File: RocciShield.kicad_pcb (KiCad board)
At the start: 2 copper layers, 176 parts, among them J1 Battery, J10 M3, J11 I2C6, J12 M4, J13 I2C7, J14 Power, J2 I2C0, J3 I2C1, J4 I2C2, J5 I2C3, J6 M1, J7 I2C4, J8 M2, J9 I2C5, Q1 IRF7416, U1 LMR33630, U2 AMS1117-3.3, U3 L7808, U4 TPS3700, U5 TCA9548A, U6 DRV8871, U7 DRV8871, U8 DRV8871, U9 DRV8871

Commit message: change linear regulator to lm317 (jlc basic part)
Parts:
- removed F10, F12, F13, F15, F16, F18, F19, F21, F22, F24, F25, F3, F4, F6, F7, F9: 10 mA, Fuse:Fuse_0805_2012Metric
- removed U3: L7808, Package_TO_SOT_SMD:SOT-223-3_TabPin2
- added R62: 1k, Resistor_SMD:R_0603_1608Metric, F.Cu at (205.5, 64.5)
- added U10: LM317_TO-252, Package_TO_SOT_SMD:TO-252-2, F.Cu at (210.4, 59.2)
- C1: value 10µ -> 22µ
- C13: value 100µ -> 22µ
- F1, F11, F14, F17, F20, F23, F5, F8: value 100 mA -> 1 A
- R12: value 200 -> 330
- R13: value 20 -> 150
- R28: value 20 -> 270
- U2: value AMS1117-3.3 -> LM317_TO-252; footprint Package_TO_SOT_SMD:SOT-223-3_TabPin2 -> Package_TO_SOT_SMD:TO-252-2
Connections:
- D17 pad 2: ERROR_LED -> +5V
- R28 pad 2: GND -> Net-(Q2-S)
- U2 pad 1: GND -> Net-(U2-ADJ)

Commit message: added changes from #2
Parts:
- removed F14, F17, F20, F23: 1 A, Fuse:Fuse_0805_2012Metric
- removed F26: 3A, Fuse:Fuse_1812_4532Metric
- removed F27: 1A, Fuse:Fuse_1812_4532Metric
- removed U10: LM317_TO-252, Package_TO_SOT_SMD:TO-252-2
- added C19: 100n, Capacitor_SMD:C_0603_1608Metric, F.Cu at (139.8, 54.3)
- added F10: 300 mA ptc, Fuse:Fuse_0805_2012Metric, F.Cu at (90.4, 143.7)
- added F3: 300 mA ptc, Fuse:Fuse_0805_2012Metric, F.Cu at (91.0, 56.1)
- added F4: 300 mA ptc, Fuse:Fuse_0805_2012Metric, F.Cu at (91.0, 70.7)
- added F6: 300 mA ptc, Fuse:Fuse_0805_2012Metric, F.Cu at (90.4, 100.5)
- added F7: 300 mA ptc, Fuse:Fuse_0805_2012Metric, F.Cu at (90.4, 115.1)
- added F9: 3A ptc, Fuse:Fuse_2920_7451Metric, F.Cu at (35.8, 143.7)
- added Q2: 2N7002, Package_TO_SOT_SMD:SOT-23, F.Cu at (28.1, 117.7)
- added R42: 1k, Resistor_SMD:R_0603_1608Metric, F.Cu at (248.7, 104.8)
- added R43: 30k, Resistor_SMD:R_0805_2012Metric, F.Cu at (240.4, 109.2)
- added R44: 4k7, Resistor_SMD:R_0603_1608Metric, F.Cu at (65.6, 120.2)
- added R45: 4k7, Resistor_SMD:R_0603_1608Metric, F.Cu at (69.4, 120.2)
- added R46: 1k, Resistor_SMD:R_0603_1608Metric, F.Cu at (31.9, 120.9)
- added R47: 100, Resistor_SMD:R_0603_1608Metric, F.Cu at (85.3, 123.4)
- added R48: 100, Resistor_SMD:R_0603_1608Metric, F.Cu at (85.3, 126.6)
- added R49: 1k, Resistor_SMD:R_0603_1608Metric, F.Cu at (244.8, 120.0)
- added R50: 1k, Resistor_SMD:R_0603_1608Metric, F.Cu at (248.7, 120.0)
- added R51: 30k, Resistor_SMD:R_0805_2012Metric, F.Cu at (240.4, 124.5)
- added R52: 4k7, Resistor_SMD:R_0603_1608Metric, F.Cu at (65.6, 134.2)
- added R53: 4k7, Resistor_SMD:R_0603_1608Metric, F.Cu at (69.4, 134.2)
- added R54: 100, Resistor_SMD:R_0603_1608Metric, F.Cu at (85.3, 137.4)
- added R55: 100, Resistor_SMD:R_0603_1608Metric, F.Cu at (85.3, 140.5)
- added R56: 1k, Resistor_SMD:R_0603_1608Metric, F.Cu at (244.8, 134.6)
- added R57: 1k, Resistor_SMD:R_0603_1608Metric, F.Cu at (248.7, 134.6)
- added R58: 30k, Resistor_SMD:R_0805_2012Metric, F.Cu at (240.4, 139.1)
- added R59: 4k7, Resistor_SMD:R_0603_1608Metric, F.Cu at (65.6, 148.8)
- added R60: 4k7, Resistor_SMD:R_0603_1608Metric, F.Cu at (69.4, 148.8)
- added R61: 100, Resistor_SMD:R_0603_1608Metric, F.Cu at (85.3, 152.0)
- added U3: LM317_TO-252, Package_TO_SOT_SMD:TO-252-2, F.Cu at (233.2, 59.7)
- C1: value 22µ -> 33µ; footprint Capacitor_SMD:CP_Elec_5x3 -> Capacitor_Tantalum_SMD:CP_EIA-7343-43_Kemet-X
- C10, C4, C5: value 22 µF -> 33µ; footprint Capacitor_SMD:CP_Elec_5x3 -> Capacitor_Tantalum_SMD:CP_EIA-7343-43_Kemet-X
- C13: value 22µ -> 33µ; footprint Capacitor_SMD:C_0603_1608Metric -> Capacitor_Tantalum_SMD:CP_EIA-7343-43_Kemet-X
- C7: footprint Capacitor_SMD:CP_Elec_5x3 -> Capacitor_SMD:C_0603_1608Metric
- D26: value GR -> 3V4; footprint LED_SMD:LED_0603_1608Metric -> Diode_SMD:D_MiniMELF
- D27: value GR -> 5V1; footprint LED_SMD:LED_0603_1608Metric -> Diode_SMD:D_MiniMELF
- D28, D29: value BAT42 -> GR; footprint Diode_SMD:D_SOD-123 -> LED_SMD:LED_0603_1608Metric
- D30: value 5V1 -> BAT42; footprint LED_SMD:LED_0603_1608Metric -> Diode_SMD:D_SOD-123
- D31: value 3V4 -> BAT42; footprint LED_SMD:LED_0603_1608Metric -> Diode_SMD:D_SOD-123
- F1, F5, F8: value 1 A -> 300 mA ptc
- F11: value 1 A -> 1A ptc; footprint Fuse:Fuse_0805_2012Metric -> Fuse:Fuse_1206_3216Metric
- J12: value M4 -> Power; footprint Connector_PinHeader_2.54mm:PinHeader_1x02_P2.54mm_Vertical -> Connector_PinHeader_2.54mm:PinHeader_1x04_P2.54mm_Vertical
- J13: value I2C7 -> M4; footprint Connector_PinHeader_2.54mm:PinHeader_1x04_P2.54mm_Vertical -> Connector_PinHeader_2.54mm:PinHeader_1x02_P2.54mm_Vertical
- J14: value Power -> I2C7
- L1: footprint Inductor_SMD:L_6.3x6.3_H3 -> Inductor_SMD:L_Sunlord_SWPA4020S
- R10: value 383k 1% -> 4k7
- R11: value 10k -> 4k7
- R12: value 330 -> 100
- R13: value 150 -> 4700k 1%
- R14: value 1k -> 10k
- R15: value 1k47 1% -> 100
- R16, R41: value 4k7 -> 1k
- R17: value 4k7 -> 330
- R18: value 14k3 1% -> 150
- R19: value 4k7 -> 10k 1%
- R20: value 4k7 -> 240
- R21: value 1k -> 240
- R22, R37: value 1k -> 4k7
- R23, R29: value 30k -> 4k7
- R24: value 4k7 -> 390
- R25: value 4k7 -> 1k3
- R26: value 1k -> 180k 1%
- R27, R32, R38, R62: value 1k -> 100
- R28: value 270 -> 100
- R3, R4: value 100k -> 100
- R31: value 4k7 -> 100
- R34: value 30k -> 1k
- R35: value 4k7 -> 30k; footprint Resistor_SMD:R_0603_1608Metric -> Resistor_SMD:R_0805_2012Metric
- R39: value 30k -> 100
- R40: value 4k7 -> 270
- R5: value 24.9k -> 100k
- R6: value 4k7 -> 100k
- R7: value 4k7 -> 24.9k
- moved D26 229.5 mm to (21.8, 148.2)
- moved D27 228.9 mm to (26.2, 148.2)
- moved J12 220.3 mm to (41.5, 143.7)
- moved R7 206.4 mm to (231.9, 50.2)
- moved R22 189.7 mm to (65.0, 75.8)
- moved R41 189.3 mm to (244.8, 104.8)
- moved R35 187.2 mm to (240.4, 94.6)
- moved R6 185.5 mm to (205.9, 47.6)
- moved R37 182.6 mm to (69.4, 105.6)
- moved R29 181.6 mm to (65.0, 91.0)
- moved R23 177.9 mm to (68.8, 75.8)
- moved R25 176.6 mm to (233.2, 66.7)
- moved D28 174.5 mm to (244.8, 139.7)
- moved D29 173.2 mm to (248.7, 139.7)
- moved R27 170.8 mm to (84.6, 79.0)
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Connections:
- C11 pad 1: GND -> +3V3
- C11 pad 2: +12V -> GND
- C12 pad 1: GND -> +8V
- C12 pad 2: +8V -> GND
- C18 pad 1: GND -> +8V
- C18 pad 2: +8V -> GND
- C3 pad 1: /SW -> /Boot
- C3 pad 2: /Boot -> /SW
- C6 pad 1: GND -> +5V
- C6 pad 2: +5V -> GND
- C8 pad 1: GND -> +5V
- C8 pad 2: +5V -> GND
- C9 pad 1: GND -> +12V
- C9 pad 2: +3V3 -> GND
- D26 pad 1: Net-(D26-K) -> +3V3
- D26 pad 2: /M4_2 -> GND
- D27 pad 1: /M4_2 -> +5V
- D27 pad 2: Net-(D27-A) -> GND
- D28 pad 1: +5V -> Net-(D28-K)
- D28 pad 2: Net-(D28-A) -> /M4_2
- D29 pad 1: +5V -> /M4_2
- D30 pad 2: GND -> Net-(D30-A)
- D31 pad 1: +3V3 -> +5V
- D31 pad 2: GND -> Net-(D31-A)
- D6 pad 2: +5V -> +12V
- D7 pad 2: +3V3 -> +5V
- D8 pad 2: +12V -> +3V3
- F11 pad 1: Net-(JP4-C) -> +3V3
- F11 pad 2: Net-(J5-Pin_4) -> Net-(J12-Pin_3)
- F5 pad 1: Net-(JP2-C) -> Net-(JP4-C)
- F5 pad 2: Net-(J3-Pin_4) -> Net-(J5-Pin_4)
- F8 pad 1: Net-(JP3-C) -> Net-(JP10-C)
- F8 pad 2: Net-(J4-Pin_4) -> Net-(J11-Pin_4)
- J12 pad 1: /M4_2 -> +12V
- J12 pad 2: /M4_1 -> Net-(J12-Pin_2)
- J13 pad 1: GND -> /M4_2
- J13 pad 2: Net-(J13-Pin_2) -> /M4_1
- J14 pad 1: +12V -> GND
- J14 pad 4: GND -> Net-(J14-Pin_4)
- R10 pad 1: /12V_after_fuse -> Net-(JP2-C)
- R10 pad 2: ADC_BAT -> Net-(D5-A)
- R11 pad 1: /12V_after_fuse -> Net-(JP2-C)
- R11 pad 2: Net-(Q1-G) -> Net-(D4-A)
- R12 pad 1: Net-(D6-K) -> Net-(D4-A)
- R12 pad 2: GND -> Net-(J3-Pin_3)
- R13 pad 1: Net-(D7-K) -> /12V_after_fuse
- R13 pad 2: GND -> ADC_BAT
- R14 pad 1: Net-(D8-K) -> /12V_after_fuse
- R14 pad 2: GND -> Net-(Q1-G)
- R15 pad 1: ADC_BAT -> Net-(D5-A)
- R15 pad 2: Net-(U4-INB-) -> Net-(J3-Pin_2)
- R16 pad 1: Net-(JP3-C) -> Net-(D6-K)
- R16 pad 2: Net-(D10-A) -> GND
- R17 pad 1: Net-(JP3-C) -> Net-(D7-K)
- R17 pad 2: Net-(D9-A) -> GND
- R18 pad 1: Net-(U4-INB-) -> Net-(D8-K)
- R19 pad 1: Net-(JP4-C) -> ADC_BAT
- R19 pad 2: Net-(D12-A) -> Net-(U4-INB-)
- R20 pad 1: Net-(JP4-C) -> Net-(U2-ADJ)
- R20 pad 2: Net-(D11-A) -> +3V3
- R21 pad 1: /M1_1 -> Net-(U3-ADJ)
- R21 pad 2: Net-(D13-K) -> +8V
- R22 pad 1: /M1_1 -> Net-(JP3-C)
- R22 pad 2: Net-(D14-A) -> Net-(D10-A)
- R23 pad 1: Net-(U6-ILIM) -> Net-(JP3-C)
- R23 pad 2: GND -> Net-(D9-A)
- R24 pad 1: Net-(JP8-C) -> GND
- R24 pad 2: Net-(D16-A) -> Net-(U2-ADJ)
- R25 pad 1: Net-(JP8-C) -> GND
- R25 pad 2: Net-(D15-A) -> Net-(U3-ADJ)
- R26 pad 1: /M2_1 -> Net-(U4-INB-)
- R26 pad 2: Net-(D18-K) -> GND
- R27 pad 1: /M2_1 -> Net-(D9-A)
- R27 pad 2: Net-(D19-A) -> Net-(J4-Pin_3)
- R28 pad 1: Net-(D17-K) -> Net-(D10-A)
- R28 pad 2: Net-(Q2-S) -> Net-(J4-Pin_2)
- R29 pad 1: Net-(U7-ILIM) -> Net-(JP4-C)
- R29 pad 2: GND -> Net-(D12-A)
- R3 pad 1: +5V -> Net-(D1-A)
- R3 pad 2: /FB -> Net-(J2-Pin_3)
- R30 pad 1: Net-(JP9-C) -> Net-(JP4-C)
- R30 pad 2: Net-(D21-A) -> Net-(D11-A)
- R31 pad 1: Net-(JP9-C) -> Net-(D11-A)
- R31 pad 2: Net-(D20-A) -> Net-(J5-Pin_3)
- R32 pad 1: /M3_1 -> Net-(D12-A)
- R32 pad 2: Net-(D22-K) -> Net-(J5-Pin_2)
- R33 pad 1: /M3_1 -> /M1_1
- R33 pad 2: Net-(D23-A) -> Net-(D13-K)
- R34 pad 1: Net-(U8-ILIM) -> /M1_1
- R34 pad 2: GND -> Net-(D14-A)
- R35 pad 1: Net-(JP10-C) -> Net-(U6-ILIM)
- R35 pad 2: Net-(D25-A) -> GND
- R36 pad 1: Net-(JP10-C) -> Net-(JP8-C)
- R36 pad 2: Net-(D24-A) -> Net-(D16-A)
- R37 pad 1: /M4_1 -> Net-(JP8-C)
- R37 pad 2: Net-(D26-K) -> Net-(D15-A)
- R38 pad 1: /M4_1 -> Net-(D15-A)
- R38 pad 2: Net-(D27-A) -> Net-(J7-Pin_3)
- R39 pad 1: Net-(U9-ILIM) -> Net-(D16-A)
- R39 pad 2: GND -> Net-(J7-Pin_2)
- R4 pad 1: Net-(U1-VCC) -> Net-(D2-A)
- R4 pad 2: /PG -> Net-(J2-Pin_2)
- R40 pad 1: Net-(JP11-C) -> Net-(D17-K)
- R40 pad 2: Net-(D29-A) -> Net-(Q2-S)
- R41 pad 1: Net-(JP11-C) -> /M2_1
- R41 pad 2: Net-(D28-A) -> Net-(D18-K)
- R5 pad 1: /FB -> +5V
- R5 pad 2: GND -> /FB
- R6 pad 1: IOREF -> Net-(U1-VCC)
- R6 pad 2: I2C_SDA -> /PG
- R62 pad 1: ERROR_LED -> Net-(D31-A)
- R62 pad 2: GND -> Net-(J14-Pin_2)
- R7 pad 1: IOREF -> /FB
- R7 pad 2: I2C_SCL -> GND
- R8 pad 1: Net-(JP2-C) -> IOREF
- R8 pad 2: Net-(D5-A) -> I2C_SDA
- R9 pad 1: Net-(JP2-C) -> IOREF
- R9 pad 2: Net-(D4-A) -> I2C_SCL
- U5 pad 19: Net-(D29-A) -> Net-(D31-A)
- U5 pad 20: Net-(D28-A) -> Net-(D30-A)

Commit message: finished JLCPCB selection and fixed isse #3
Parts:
- added C20: 100n, Capacitor_SMD:C_0603_1608Metric, F.Cu at (102.2, 110.5)
- added R63: 100, Resistor_SMD:R_0603_1608Metric, F.Cu at (76.2, 124.5)
- added R64: 100, Resistor_SMD:R_0603_1608Metric, F.Cu at (76.2, 127.6)
- C1: value 33µ -> 100µ; footprint Capacitor_Tantalum_SMD:CP_EIA-7343-43_Kemet-X -> Package_TO_SOT_SMD:SOT-23
- C10, C13: value 33µ -> 100n; footprint Capacitor_Tantalum_SMD:CP_EIA-7343-43_Kemet-X -> Capacitor_SMD:C_0603_1608Metric
- C11, C14: value 100n -> 100µ; footprint Capacitor_SMD:C_0603_1608Metric -> Capacitor_SMD:CP_Elec_6.3x7.7
- Q1: value IRF7416 -> IRF7404; footprint Package_SO:SO-8_5.3x6.2mm_P1.27mm -> Package_SO:SOIC-8_3.9x4.9mm_P1.27mm
- R29: value 4k7 -> 300k 1%
- R31, R38, R39, R47, R54, R55, R61, R62: value 100 -> 4k7
- R32: value 100 -> 100k 1%
- R33, R34, R41, R49, R50, R56, R57: value 1k -> 100
- R35, R43, R51, R58: value 30k -> 1k; footprint Resistor_SMD:R_0805_2012Metric -> Resistor_SMD:R_0603_1608Metric
- R36, R44, R52, R59: value 4k7 -> 1k
- R37, R45, R53, R60: value 4k7 -> 30k; footprint Resistor_SMD:R_0603_1608Metric -> Resistor_SMD:R_0805_2012Metric
- R40: value 270 -> 100
- R42: value 1k -> 270
- R46: value 1k -> 4k7
- R48: value 100 -> 10k
- moved R42 231.7 mm to (17.8, 85.1)
- moved R36 194.6 mm to (257.0, 70.6)
- moved R44 194.6 mm to (257.0, 85.2)
- moved R52 194.4 mm to (257.0, 100.5)
- moved R59 194.4 mm to (257.0, 115.1)
- moved R37 182.0 mm to (248.8, 75.1)
- moved R45 182.0 mm to (248.8, 89.7)
- moved R53 181.8 mm to (248.8, 104.9)
- moved R60 181.8 mm to (248.8, 119.5)
- moved R34 174.3 mm to (75.6, 69.8)
- moved R57 173.8 mm to (76.2, 113.0)
- moved R50 173.7 mm to (76.2, 99.1)
- moved R33 170.9 mm to (75.6, 66.7)
- moved R56 170.5 mm to (76.2, 109.9)
- moved R49 170.4 mm to (76.2, 95.9)
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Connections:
- C1 pad 1: +12V -> +12VA
- C12 pad 1: +8V -> +12VA
- C13 pad 1: +12V -> +8V
- C18 pad 1: +8V -> +12V
- C19 pad 1: /12V_after_fuse -> GND
- C19 pad 2: GND -> ADC_BAT
- C2 pad 1: +12V -> +12VA
- C8 pad 1: +5V -> +12V
- C9 pad 1: +12V -> +5V
- D3 pad 1: /12V_after_fuse -> +12V
- D6 pad 2: +12V -> +12VA
- F2 pad 2: /12V_after_fuse -> +12V
- Q1 pad 1: Net-(Q1-G) -> +12VA
- Q1 pad 2: /12V_after_fuse -> +12VA
- Q1 pad 3: +12V -> +12VA
- Q1 pad 4: (no net) -> Net-(Q1-G)
- Q1 pad 5: (no net) -> +12V
- Q1 pad 6: (no net) -> +12V
- Q1 pad 7: (no net) -> +12V
- Q1 pad 8: (no net) -> +12V
- Q2 pad 2: GND -> Net-(Q2-S)
- Q2 pad 3: Net-(Q2-S) -> GND
- R13 pad 1: /12V_after_fuse -> +12V
- R13 pad 2: ADC_BAT -> Net-(U4-INA+)
- R14 pad 1: /12V_after_fuse -> +12V
- R19 pad 1: ADC_BAT -> Net-(U4-INA+)
- R29 pad 1: Net-(JP4-C) -> +12VA
- R29 pad 2: Net-(D12-A) -> ADC_BAT
- R30 pad 2: Net-(D11-A) -> Net-(D12-A)
- R31 pad 1: Net-(D11-A) -> Net-(JP4-C)
- R31 pad 2: Net-(J5-Pin_3) -> Net-(D11-A)
- R32 pad 1: Net-(D12-A) -> ADC_BAT
- R32 pad 2: Net-(J5-Pin_2) -> GND
- R33 pad 1: /M1_1 -> Net-(D11-A)
- R33 pad 2: Net-(D13-K) -> Net-(J5-Pin_3)
- R34 pad 1: /M1_1 -> Net-(D12-A)
- R34 pad 2: Net-(D14-A) -> Net-(J5-Pin_2)
- R35 pad 1: Net-(U6-ILIM) -> /M1_1
- R35 pad 2: GND -> Net-(D13-K)
- R36 pad 1: Net-(JP8-C) -> /M1_1
- R36 pad 2: Net-(D16-A) -> Net-(D14-A)
- R37 pad 1: Net-(JP8-C) -> Net-(U6-ILIM)
- R37 pad 2: Net-(D15-A) -> GND
- R38 pad 1: Net-(D15-A) -> Net-(JP8-C)
- R38 pad 2: Net-(J7-Pin_3) -> Net-(D16-A)
- R39 pad 1: Net-(D16-A) -> Net-(JP8-C)
- R39 pad 2: Net-(J7-Pin_2) -> Net-(D15-A)
- R40 pad 1: Net-(D17-K) -> Net-(D15-A)
- R40 pad 2: Net-(Q2-S) -> Net-(J7-Pin_3)
- R41 pad 1: /M2_1 -> Net-(D16-A)
- R41 pad 2: Net-(D18-K) -> Net-(J7-Pin_2)
- R42 pad 1: /M2_1 -> Net-(D17-K)
- R42 pad 2: Net-(D19-A) -> Net-(Q2-S)
- R43 pad 1: Net-(U7-ILIM) -> /M2_1
- R43 pad 2: GND -> Net-(D18-K)
- R44 pad 1: Net-(JP9-C) -> /M2_1
- R44 pad 2: Net-(D21-A) -> Net-(D19-A)
- R45 pad 1: Net-(JP9-C) -> Net-(U7-ILIM)
- R45 pad 2: Net-(D20-A) -> GND
- R46 pad 1: ERROR_LED -> Net-(JP9-C)
- R46 pad 2: GND -> Net-(D21-A)
- R47 pad 1: Net-(D20-A) -> Net-(JP9-C)
- R47 pad 2: Net-(J9-Pin_3) -> Net-(D20-A)
- R48 pad 1: Net-(D21-A) -> ERROR_LED
- R48 pad 2: Net-(J9-Pin_2) -> GND
- R49 pad 1: /M3_1 -> Net-(D20-A)
- R49 pad 2: Net-(D22-K) -> Net-(J9-Pin_3)
- R50 pad 1: /M3_1 -> Net-(D21-A)
- R50 pad 2: Net-(D23-A) -> Net-(J9-Pin_2)
- R51 pad 1: Net-(U8-ILIM) -> /M3_1
- R51 pad 2: GND -> Net-(D22-K)
- R52 pad 1: Net-(JP10-C) -> /M3_1
- R52 pad 2: Net-(D25-A) -> Net-(D23-A)
- R53 pad 1: Net-(JP10-C) -> Net-(U8-ILIM)
- R53 pad 2: Net-(D24-A) -> GND
- R54 pad 1: Net-(D24-A) -> Net-(JP10-C)
- R54 pad 2: Net-(J11-Pin_3) -> Net-(D25-A)
- R55 pad 1: Net-(D25-A) -> Net-(JP10-C)
- R55 pad 2: Net-(J11-Pin_2) -> Net-(D24-A)
- R56 pad 1: /M4_1 -> Net-(D24-A)
- R56 pad 2: Net-(D28-K) -> Net-(J11-Pin_3)
- R57 pad 1: /M4_1 -> Net-(D25-A)
- R57 pad 2: Net-(D29-A) -> Net-(J11-Pin_2)
- R58 pad 1: Net-(U9-ILIM) -> /M4_1
- R58 pad 2: GND -> Net-(D28-K)
- R59 pad 1: Net-(JP11-C) -> /M4_1
- R59 pad 2: Net-(D31-A) -> Net-(D29-A)
- R60 pad 1: Net-(JP11-C) -> Net-(U9-ILIM)
- R60 pad 2: Net-(D30-A) -> GND
- R61 pad 1: Net-(D30-A) -> Net-(JP11-C)
- R61 pad 2: Net-(J14-Pin_3) -> Net-(D31-A)
- R62 pad 1: Net-(D31-A) -> Net-(JP11-C)
- R62 pad 2: Net-(J14-Pin_2) -> Net-(D30-A)
- TP7 pad 1: /12V_after_fuse -> +12V
- U1 pad 2: +12V -> +12VA
- U1 pad 3: +12V -> +12VA
- U3 pad 3: +12V -> +12VA
- U4 pad 3: ADC_BAT -> Net-(U4-INA+)
- U4 pad 5: /12V_after_fuse -> +12V

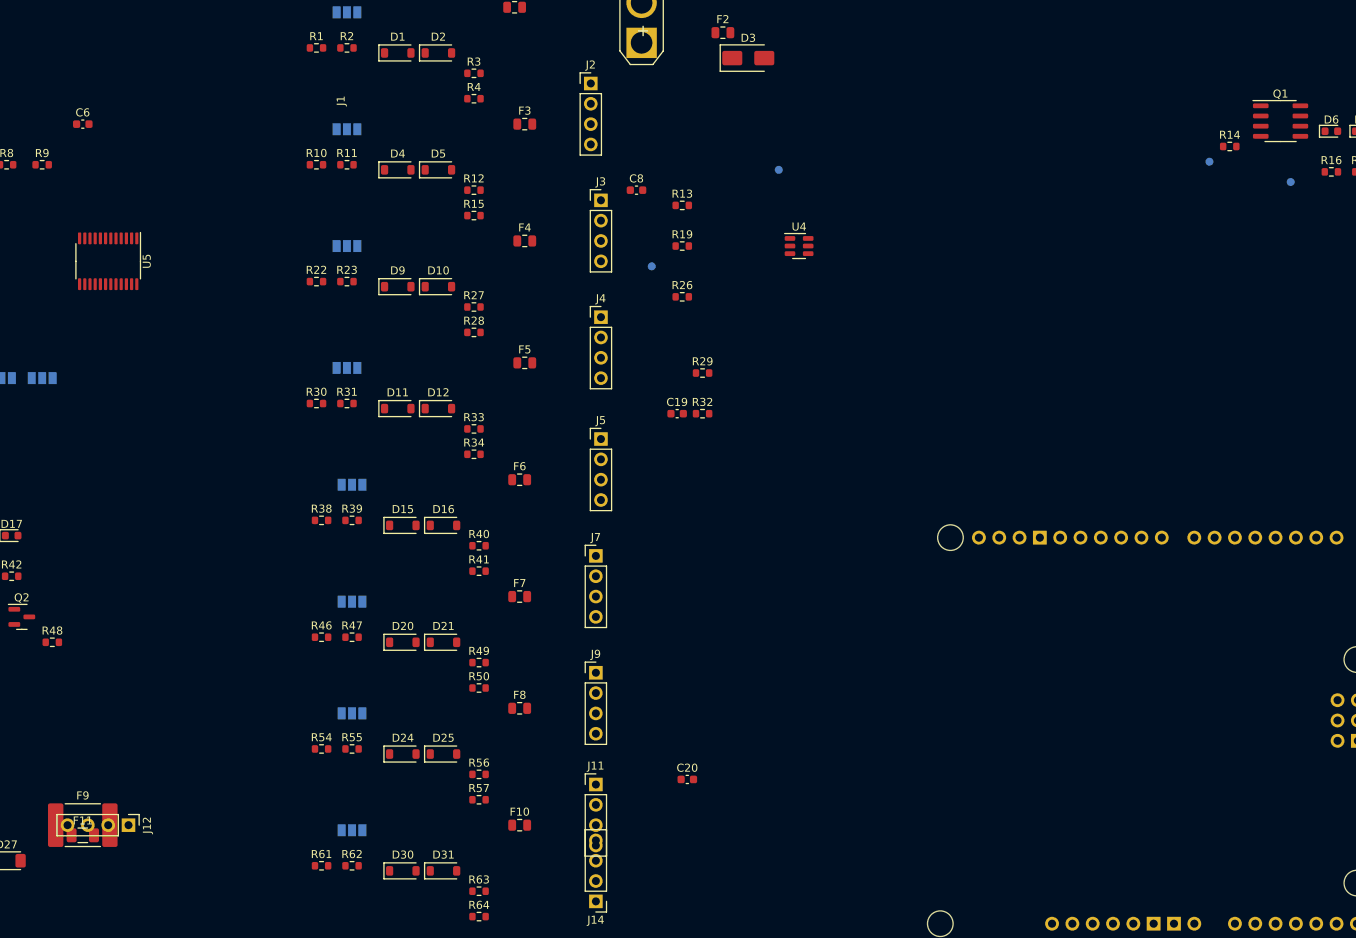
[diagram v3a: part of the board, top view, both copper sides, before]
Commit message: added more TODOs
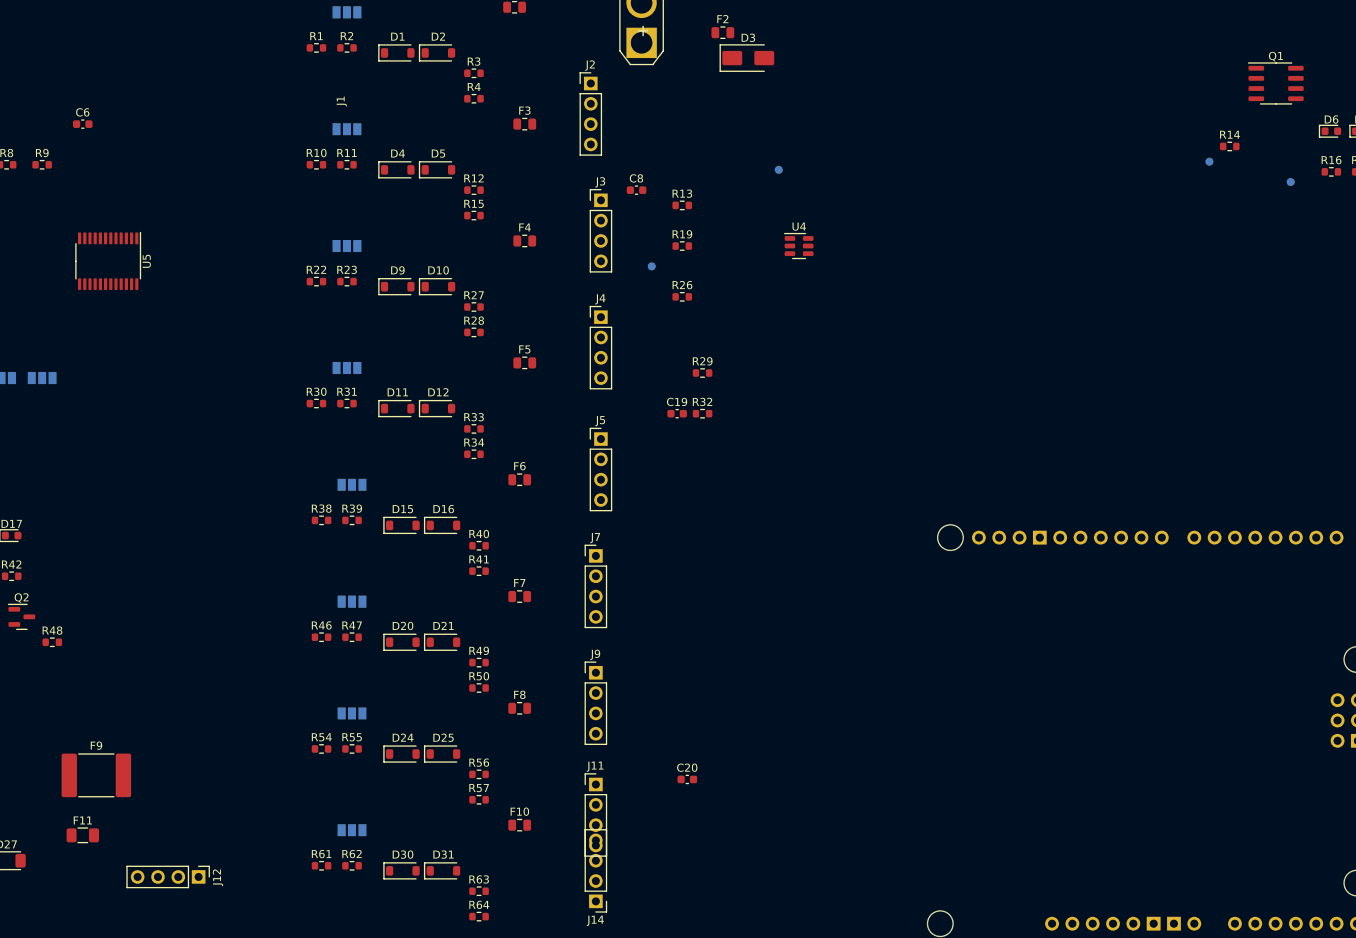
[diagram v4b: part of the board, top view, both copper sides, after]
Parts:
- moved J12 10.9 mm to (41.1, 122.7)
- moved F9 6.45 mm to (28.4, 110.0)
- moved Q1 4.73 mm to (175.8, 23.5)
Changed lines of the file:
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@@
   )
   (setup
+    (stackup
+      (layer "F.SilkS" (type "Top Silk Screen"))
+      (layer "F.Paste" (type "Top Solder Paste"))
+      (layer "F.Mask" (type "Top Solder Mask") (thickness 0.01))
+      (layer "F.Cu" (type "copper") (thickness 0.035))
+      (layer "dielectric 1" (type "core") (thickness 1.51) (material "FR4") (epsilon_r 4.5) (loss_tangent 0.02))
+      (layer "B.Cu" (type "copper") (thickness 0.035))
+      (layer "B.Mask" (type "Bottom Solder Mask") (thickness 0.01))
+      (layer "B.Paste" (type "Bottom Solder Paste"))
+      (layer "B.SilkS" (type "Bottom Silk Screen"))
+      (copper_finish "None")
+      (dielectric_constraints no)
+    )
     (pad_to_mask_clearance 0)
     (pcbplotparams
@@
   )
   (footprint "Fuse:Fuse_2920_7451Metric" (layer "F.Cu")
-    (at 26.67 116.205)
+    (at 28.3625 109.982)
     (descr "Fuse SMD 2920 (7451 Metric), square (rectangular) end terminal, IPC_7351 nominal, (Body size from: http://www.megastar.com/products/fusetronic/polyswitch/PDF/smd2920.pdf), generated with kicad-footprint-generator")
     (tags "fuse")
@@
   )
   (footprint "Connector_PinHeader_2.54mm:PinHeader_1x04_P2.54mm_Vertical" (layer "F.Cu")
-    (at 32.385 116.205 -90)
+    (at 41.148 122.682 -90)
     (descr "Through hole straight pin header, 1x04, 2.54mm pitch, single row")
     (tags "Through hole pin header THT 1x04 2.54mm single row")
@@
   )
   (footprint "Package_SO:SOIC-8_3.9x4.9mm_P1.27mm" (layer "F.Cu")
-    (at 176.39 28.194)
+    (at 175.833 23.495)
     (descr "SOIC, 8 Pin (JEDEC MS-012AA, https://www.analog.com/media/en/package-pcb-resources/package/pkg_pdf/soic_narrow-r/r_8.pdf), generated with kicad-footprint-generator ipc_gullwing_generator.py")
     (tags "SOIC SO")
@@
     (descr "Fuse SMD 0805 (2012 Metric), square (rectangular) end terminal, IPC_7351 nominal, (Body size source: https://docs.google.com/spreadsheets/d/1BsfQQcO9C6DZCsRaXUlFlo91Tg2WpOkGARC1WS5S8t0/edit?usp=sharing), generated with kicad-footprint-generator")
     (tags "fuse")
+    (property "LCSC" "C122783")
     (property "Sheetfile" "RocciShield.kicad_sch")
     (property "Sheetname" "")
